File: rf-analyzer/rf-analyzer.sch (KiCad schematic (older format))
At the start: 59 parts, among them U1 AD8302, U2 AD8302

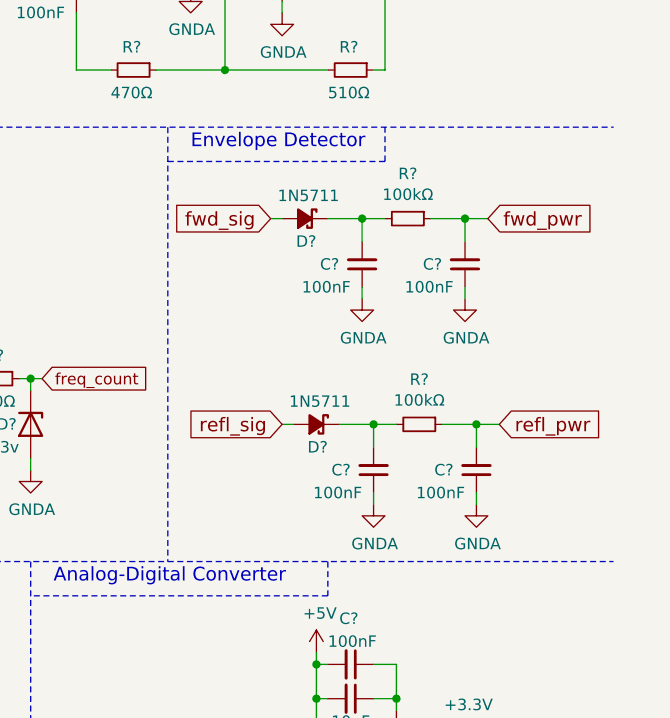
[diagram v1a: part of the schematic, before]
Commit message: Fixed bug in envelope detector that messed up DC decoupling.
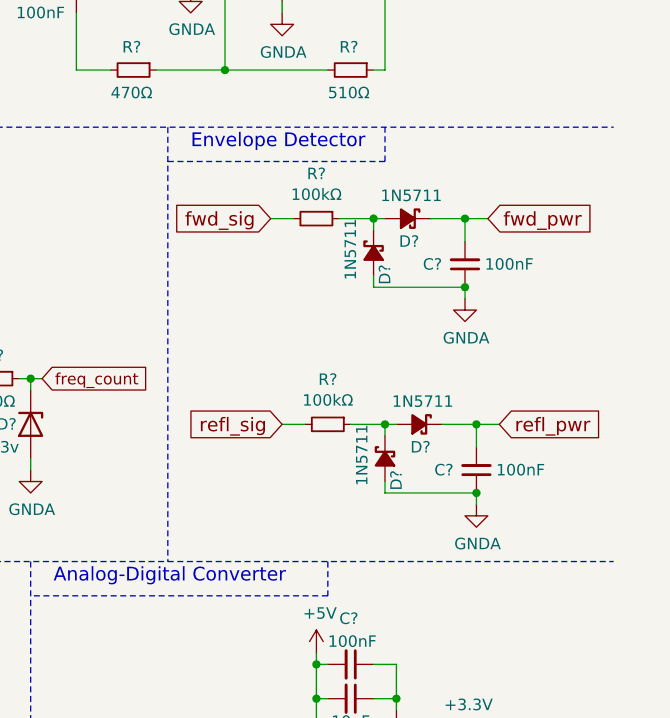
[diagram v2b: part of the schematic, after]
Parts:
- removed C? (x3): 100nF, Capacitor_SMD:C_0603_1608Metric_Pad1.05x0.95mm_HandSolder, symbol Device:C_Small
- removed D?: 1N5711, Diode_SMD:D_SMA, symbol Device:D_Schottky_Small_ALT
- removed R?: 100kΩ, Resistor_SMD:R_0603_1608Metric_Pad1.05x0.95mm_HandSolder, symbol Device:R_Small
- added C?: 100nF, Capacitor_SMD:C_0603_1608Metric_Pad1.05x0.95mm_HandSolder, symbol Device:C_Small
- added D? (x3): 1N5711, Diode_SMD:D_SMA, symbol Device:D_Schottky_Small_ALT
- added R?: 100kΩ, Resistor_SMD:R_0603_1608Metric_Pad1.05x0.95mm_HandSolder, symbol Device:R_Small
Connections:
- net GNDA: now also C?.1, D?.2 (A), D?.2 (A)
- net fwd_pwr: now also C?.2, D?.1 (K); no longer R?.1
- net fwd_sig: now also R?.2; no longer D?.2 (A)
- net refl_pwr: now also C?.2, D?.1 (K)
- net refl_sig: now also R?.2
- new net: D?.1 (K), D?.2 (A), R?.1 (x2)
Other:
- moved on the sheet: C?, D?, R?
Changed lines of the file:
@@
 L Device:D_Schottky_Small_ALT D?
 U 1 1 5970BBB4
-P 9850 2300
-F 0 "D?" H 9800 2200 50  0000 L CNN
-F 1 "1N5711" H 9700 2400 50  0000 L CNN
-F 2 "Diode_SMD:D_SMA" V 9850 2300 50  0001 C CNN
-F 3 "" V 9850 2300 50  0001 C CNN
-	1    9850 2300
+P 10300 2300
+F 0 "D?" H 10250 2200 50  0000 L CNN
+F 1 "1N5711" H 10150 2400 50  0000 L CNN
+F 2 "Diode_SMD:D_SMA" V 10300 2300 50  0001 C CNN
+F 3 "" V 10300 2300 50  0001 C CNN
+	1    10300 2300
 	-1   0    0    -1
 $EndComp
@@
 L Device:C_Small C?
 U 1 1 5970BF1F
-P 10100 2500
-F 0 "C?" H 10200 2500 50  0000 L CNN
-F 1 "100nF" H 10150 2600 50  0000 L CNN
-F 2 "Capacitor_SMD:C_0603_1608Metric_Pad1.05x0.95mm_HandSolder" H 10100 2500 50  0001 C CNN
-F 3 "" H 10100 2500 50  0001 C CNN
-	1    10100 2500
-	-1   0    0    1
-$EndComp
-$Comp
-L Device:C_Small C?
-U 1 1 5970C0BE
 P 10550 2500
 F 0 "C?" H 10650 2500 50  0000 L CNN
-F 1 "100nF" H 10600 2600 50  0000 L CNN
+F 1 "100nF" H 10250 2500 50  0000 L CNN
 F 2 "Capacitor_SMD:C_0603_1608Metric_Pad1.05x0.95mm_HandSolder" H 10550 2500 50  0001 C CNN
 F 3 "" H 10550 2500 50  0001 C CNN
@@
 Text GLabel 10650 2300 2    60   Input ~ 0
 fwd_pwr
-$Comp
-L Device:D_Schottky_Small_ALT D?
-U 1 1 5970EE87
-P 9900 3200
-F 0 "D?" H 9850 3100 50  0000 L CNN
-F 1 "1N5711" H 9750 3300 50  0000 L CNN
-F 2 "Diode_SMD:D_SMA" V 9900 3200 50  0001 C CNN
-F 3 "" V 9900 3200 50  0001 C CNN
-	1    9900 3200
-	-1   0    0    -1
-$EndComp
-$Comp
-L Device:C_Small C?
-U 1 1 5970EE8D
-P 10150 3400
-F 0 "C?" H 10250 3400 50  0000 L CNN
-F 1 "100nF" H 10200 3500 50  0000 L CNN
-F 2 "Capacitor_SMD:C_0603_1608Metric_Pad1.05x0.95mm_HandSolder" H 10150 3400 50  0001 C CNN
-F 3 "" H 10150 3400 50  0001 C CNN
-	1    10150 3400
-	-1   0    0    1
-$EndComp
-$Comp
-L Device:C_Small C?
-U 1 1 5970EE93
-P 10600 3400
-F 0 "C?" H 10700 3400 50  0000 L CNN
-F 1 "100nF" H 10650 3500 50  0000 L CNN
-F 2 "Capacitor_SMD:C_0603_1608Metric_Pad1.05x0.95mm_HandSolder" H 10600 3400 50  0001 C CNN
-F 3 "" H 10600 3400 50  0001 C CNN
-	1    10600 3400
-	-1   0    0    1
-$EndComp
 Text GLabel 9750 3200 0    60   Input ~ 0
 refl_sig
@@
 	10550 2600 10550 2650
 Wire Wire Line
-	10100 2600 10100 2650
-Wire Wire Line
-	9950 2300 10100 2300
-Wire Wire Line
-	10100 2400 10100 2300
-Connection ~ 10100 2300
-Wire Wire Line
 	10400 2300 10550 2300
 Wire Wire Line
-	10550 2300 10550 2400
+	10550 2400 10550 2300
 Connection ~ 10550 2300
-Wire Wire Line
-	10600 3500 10600 3550
-Wire Wire Line
-	10150 3500 10150 3550
-Wire Wire Line
-	10000 3200 10150 3200
-Wire Wire Line
-	10150 3300 10150 3200
-Connection ~ 10150 3200
-Wire Wire Line
-	10450 3200 10600 3200
-Wire Wire Line
-	10600 3200 10600 3300
-Connection ~ 10600 3200
 Wire Notes Line
 	9250 2050 10200 2050
@@
 	9350 950  9550 950
 Wire Wire Line
-	10100 2300 10200 2300
-Wire Wire Line
 	10550 2300 10650 2300
-Wire Wire Line
-	10150 3200 10250 3200
-Wire Wire Line
-	10600 3200 10700 3200
 Wire Wire Line
 	800  1550 800  1700
@@
 L power:GNDA #PWR0113
 U 1 1 5C552FF8
-P 10100 2650
-F 0 "#PWR0113" H 10100 2400 50  0001 C CNN
-F 1 "GNDA" H 10105 2477 50  0000 C CNN
-F 2 "" H 10100 2650 50  0001 C CNN
-F 3 "" H 10100 2650 50  0001 C CNN
-	1    10100 2650
-	1    0    0    -1
-$EndComp
-$Comp
-L power:GNDA #PWR0114
-U 1 1 5C5530D4
 P 10550 2650
-F 0 "#PWR0114" H 10550 2400 50  0001 C CNN
+F 0 "#PWR0113" H 10550 2400 50  0001 C CNN
 F 1 "GNDA" H 10555 2477 50  0000 C CNN
 F 2 "" H 10550 2650 50  0001 C CNN
 F 3 "" H 10550 2650 50  0001 C CNN
 	1    10550 2650
-	1    0    0    -1
-$EndComp
-$Comp
-L power:GNDA #PWR0116
-U 1 1 5C55328C
-P 10150 3550
-F 0 "#PWR0116" H 10150 3300 50  0001 C CNN
-F 1 "GNDA" H 10155 3377 50  0000 C CNN
-F 2 "" H 10150 3550 50  0001 C CNN
-F 3 "" H 10150 3550 50  0001 C CNN
-	1    10150 3550
-	1    0    0    -1
-$EndComp
-$Comp
-L power:GNDA #PWR0117
-U 1 1 5C553368
-P 10600 3550
-F 0 "#PWR0117" H 10600 3300 50  0001 C CNN
-F 1 "GNDA" H 10605 3377 50  0000 C CNN
-F 2 "" H 10600 3550 50  0001 C CNN
-F 3 "" H 10600 3550 50  0001 C CNN
-	1    10600 3550
 	1    0    0    -1
 $EndComp
@@
 L Device:R_Small R?
 U 1 1 5C72DFC1
-P 10300 2300
-F 0 "R?" V 10104 2300 50  0000 C CNN
-F 1 "100kΩ" V 10195 2300 50  0000 C CNN
-F 2 "Resistor_SMD:R_0603_1608Metric_Pad1.05x0.95mm_HandSolder" H 10300 2300 50  0001 C CNN
-F 3 "~" H 10300 2300 50  0001 C CNN
-	1    10300 2300
-	0    1    1    0
-$EndComp
-$Comp
-L Device:R_Small R?
-U 1 1 5C72E0F0
-P 10350 3200
-F 0 "R?" V 10154 3200 50  0000 C CNN
-F 1 "100kΩ" V 10245 3200 50  0000 C CNN
-F 2 "Resistor_SMD:R_0603_1608Metric_Pad1.05x0.95mm_HandSolder" H 10350 3200 50  0001 C CNN
-F 3 "~" H 10350 3200 50  0001 C CNN
-	1    10350 3200
+P 9900 2300
+F 0 "R?" V 9704 2300 50  0000 C CNN
+F 1 "100kΩ" V 9795 2300 50  0000 C CNN
+F 2 "Resistor_SMD:R_0603_1608Metric_Pad1.05x0.95mm_HandSolder" H 9900 2300 50  0001 C CNN
+F 3 "~" H 9900 2300 50  0001 C CNN
+	1    9900 2300
 	0    1    1    0
 $EndComp
@@
 	7450 2000 7450 2050
 Wire Wire Line
-	9750 2300 9700 2300
-Wire Wire Line
-	9800 3200 9750 3200
+	10200 2300 10150 2300
 Text GLabel 8800 950  0    60   Input ~ 0
 fwd_sig_dc
@@
 	8000 2600 8000 2700
 Connection ~ 8000 2600
+$Comp
+L Device:D_Schottky_Small_ALT D?
+U 1 1 5FE8910D
+P 10150 2450
+F 0 "D?" H 10200 2400 50  0000 L CNN
+F 1 "1N5711" H 10000 2550 50  0000 L CNN
+F 2 "Diode_SMD:D_SMA" V 10150 2450 50  0001 C CNN
+F 3 "" V 10150 2450 50  0001 C CNN
+	1    10150 2450
+	0    -1   1    0
+$EndComp
+Wire Wire Line
+	10550 2600 10150 2600
+Wire Wire Line
+	10150 2600 10150 2550
+Connection ~ 10550 2600
+Wire Wire Line
+	10150 2350 10150 2300
+Wire Wire Line
+	10000 2300 10150 2300
+Connection ~ 10150 2300
+Wire Wire Line
+	9800 2300 9700 2300
+$Comp
+L Device:D_Schottky_Small_ALT D?
+U 1 1 5FF659C1
+P 10350 3200
+F 0 "D?" H 10300 3100 50  0000 L CNN
+F 1 "1N5711" H 10200 3300 50  0000 L CNN
+F 2 "Diode_SMD:D_SMA" V 10350 3200 50  0001 C CNN
+F 3 "" V 10350 3200 50  0001 C CNN
+	1    10350 3200
+	-1   0    0    -1
+$EndComp
+$Comp
+L Device:C_Small C?
+U 1 1 5FF659C7
+P 10600 3400
+F 0 "C?" H 10700 3400 50  0000 L CNN
+F 1 "100nF" H 10300 3400 50  0000 L CNN
+F 2 "Capacitor_SMD:C_0603_1608Metric_Pad1.05x0.95mm_HandSolder" H 10600 3400 50  0001 C CNN
+F 3 "" H 10600 3400 50  0001 C CNN
+	1    10600 3400
+	-1   0    0    1
+$EndComp
+Wire Wire Line
+	10600 3500 10600 3550
+Wire Wire Line
+	10450 3200 10600 3200
+Wire Wire Line
+	10600 3300 10600 3200
+Connection ~ 10600 3200
+Wire Wire Line
+	10600 3200 10700 3200
+$Comp
+L power:GNDA #PWR?
+U 1 1 5FF659D2
+P 10600 3550
+F 0 "#PWR?" H 10600 3300 50  0001 C CNN
+F 1 "GNDA" H 10605 3377 50  0000 C CNN
+F 2 "" H 10600 3550 50  0001 C CNN
+F 3 "" H 10600 3550 50  0001 C CNN
+	1    10600 3550
+	1    0    0    -1
+$EndComp
+$Comp
+L Device:R_Small R?
+U 1 1 5FF659D8
+P 9950 3200
+F 0 "R?" V 9754 3200 50  0000 C CNN
+F 1 "100kΩ" V 9845 3200 50  0000 C CNN
+F 2 "Resistor_SMD:R_0603_1608Metric_Pad1.05x0.95mm_HandSolder" H 9950 3200 50  0001 C CNN
+F 3 "~" H 9950 3200 50  0001 C CNN
+	1    9950 3200
+	0    1    1    0
+$EndComp
+Wire Wire Line
+	10250 3200 10200 3200
+$Comp
+L Device:D_Schottky_Small_ALT D?
+U 1 1 5FF659DF
+P 10200 3350
+F 0 "D?" H 10250 3300 50  0000 L CNN
+F 1 "1N5711" H 10050 3450 50  0000 L CNN
+F 2 "Diode_SMD:D_SMA" V 10200 3350 50  0001 C CNN
+F 3 "" V 10200 3350 50  0001 C CNN
+	1    10200 3350
+	0    -1   1    0
+$EndComp
+Wire Wire Line
+	10600 3500 10200 3500
+Wire Wire Line
+	10200 3500 10200 3450
+Connection ~ 10600 3500
+Wire Wire Line
+	10200 3250 10200 3200
+Wire Wire Line
+	10050 3200 10200 3200
+Connection ~ 10200 3200
+Wire Wire Line
+	9850 3200 9750 3200
 $EndSCHEMATC

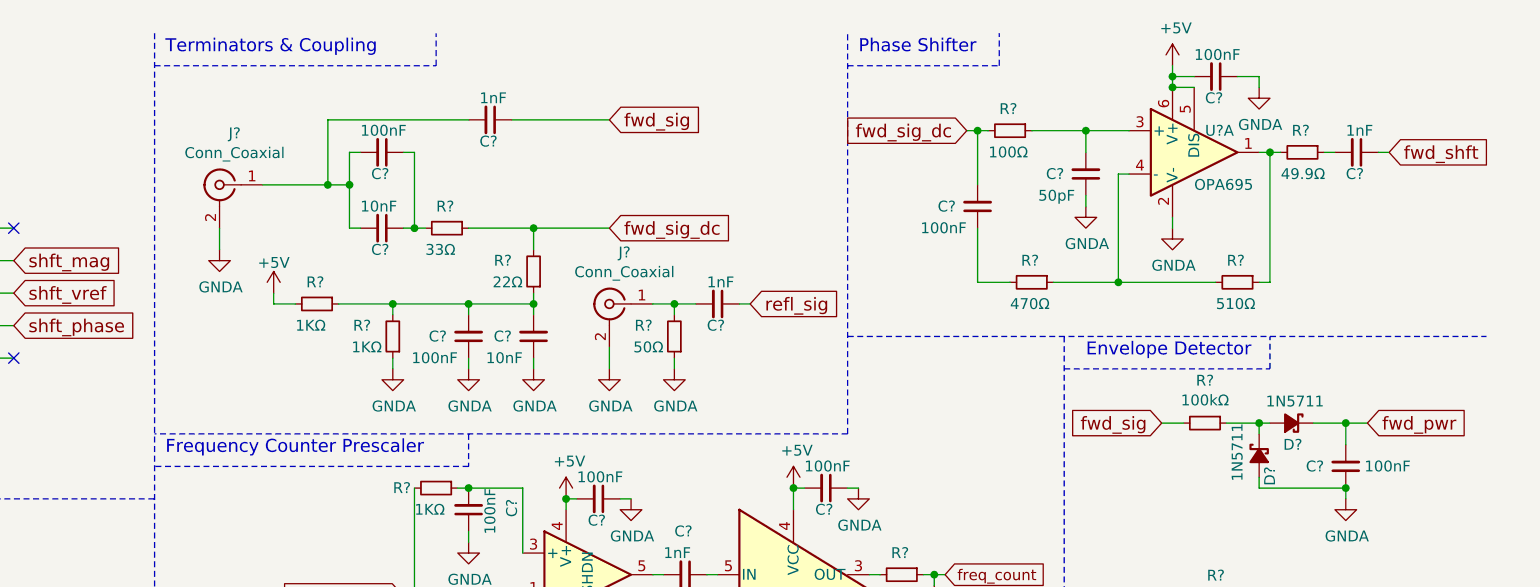
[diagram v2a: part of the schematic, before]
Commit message: Reduced the number and value of the decoupling capacitors on the DC biasing section.
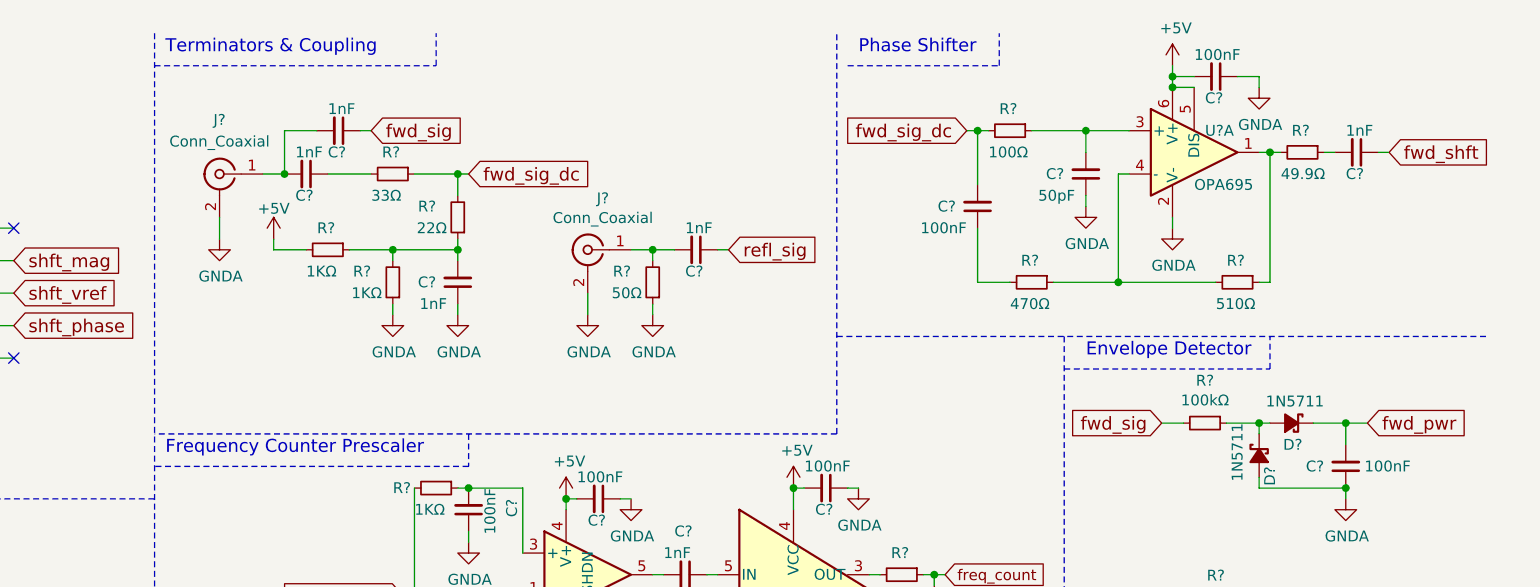
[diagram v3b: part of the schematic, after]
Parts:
- removed C? (x2): 100nF, Capacitor_SMD:C_0603_1608Metric_Pad1.05x0.95mm_HandSolder, symbol Device:C_Small
- C? (x2): value 10nF -> 1nF
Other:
- moved on the sheet: C?, J?, R?
